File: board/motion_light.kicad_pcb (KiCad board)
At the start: 2 copper layers, 35 x 63.2 mm, 18 parts, among them CON1 AVR-ISP-6, J1 MOTION, J2 Conn_02x03_Counter_Clockwise, SW1 SW_Push, SW2 SW_Push, U1 ATTINY84-SSU, U2 APA102, U3 APA102, U4 PIR_MODULE

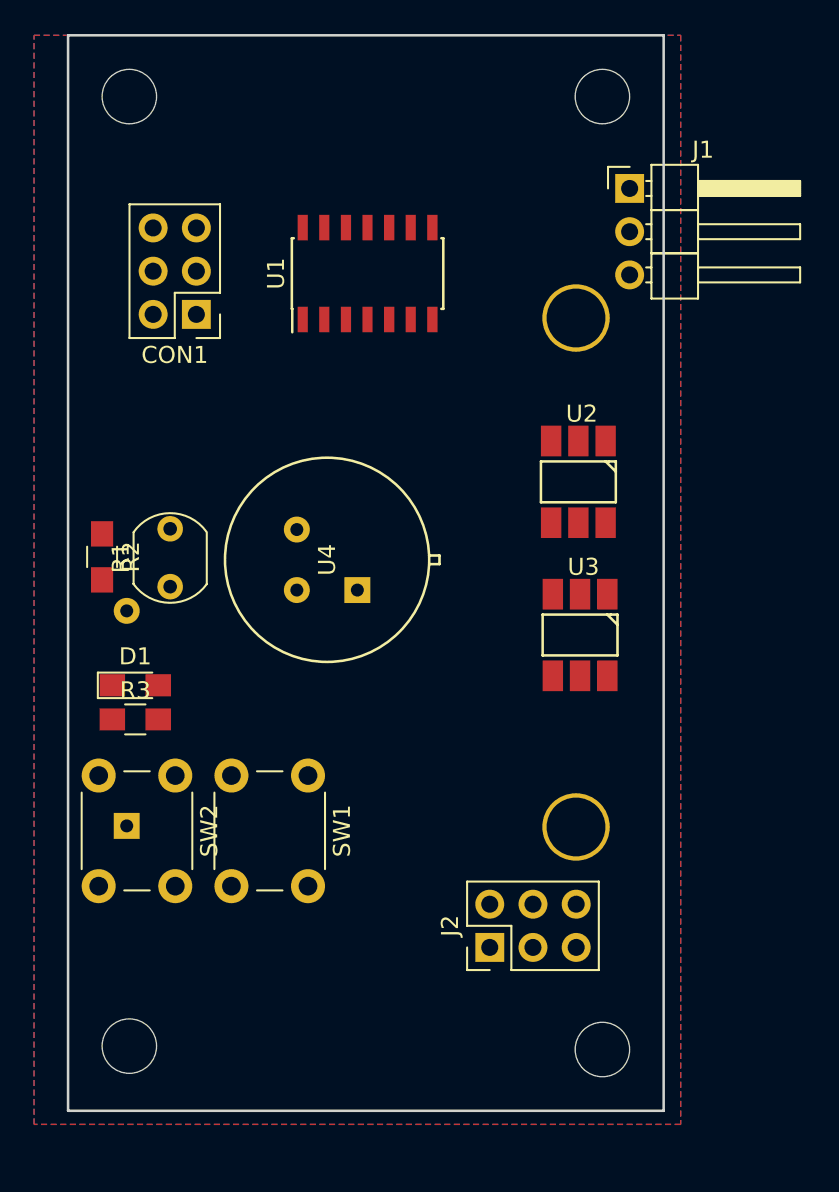
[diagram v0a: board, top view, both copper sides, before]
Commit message: Rework board; add mesh design
* Make board an even size
* Adjust position of motion detector
* Improve model of PIR sensor
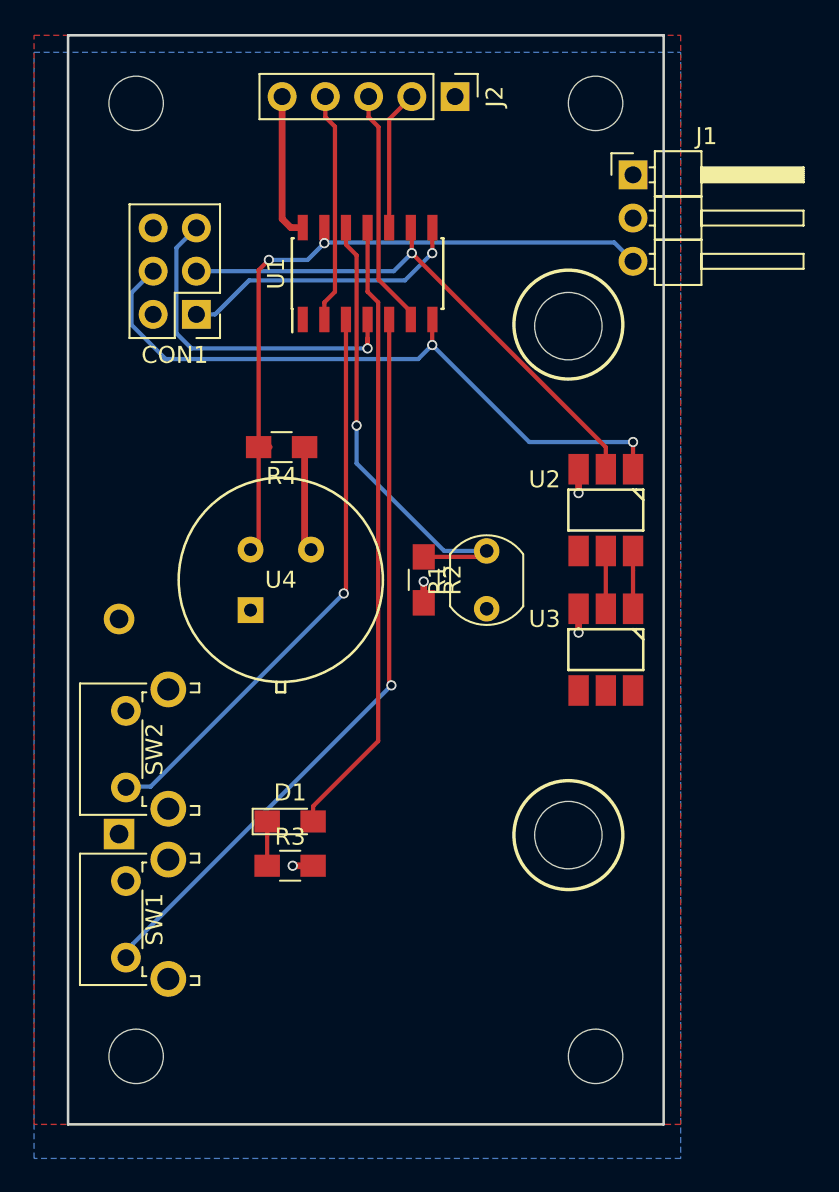
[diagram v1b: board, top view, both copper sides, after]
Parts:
- added R4: 66.5K, Resistors_SMD:R_0805_HandSoldering, F.Cu at (126.5, 84.2)
- J2: value Conn_02x03_Counter_Clockwise -> Conn_01x05; footprint Pin_Headers:Pin_Header_Straight_2x03_Pitch2.54mm -> Pin_Headers:Pin_Header_Straight_1x05_Pitch2.54mm
- SW1, SW2: footprint Buttons_Switches_THT:SW_PUSH_6mm -> Buttons_Switches_THT:SW_Tactile_SPST_Angled_PTS645Vx83-2LFS
- U1: value ATTINY84-SSU -> ATTINY84A-SSU
- moved J2 50.0 mm to (136.7, 63.6), turned to 270 degrees
- moved R2 18.9 mm to (134.9, 92.0)
- moved R1 18.6 mm to (138.6, 93.7)
- moved SW1 15.1 mm to (117.4, 114.2), turned to 90 degrees
- moved R3 12.5 mm to (127.0, 108.8)
- moved D1 12.1 mm to (127.0, 106.2)
- moved SW2 2.98 mm to (117.4, 104.2), turned to 90 degrees
- moved U4 2.97 mm to (126.5, 92.0), turned to 180 degrees
- moved U2 2.31 mm to (145.6, 87.9)
- moved U3 1.74 mm to (145.6, 96.1)
- moved J1 0.82 mm to (147.2, 68.2)
- moved REF** 0.72 mm to (118.0, 120.0)
- moved BT1 0.66 mm to (143.4, 92.0)
- moved REF** 0.57 mm to (145.0, 120.0)
- moved REF** 0.57 mm to (145.0, 64.0)
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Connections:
- J2 pad 4: GND -> /PB0
- J2 pad 5: /PB0 -> GND
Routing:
- net /BUTTON1: track 0.00 -> 43.4 mm, vias 0 -> 1
- net /MOTION: track 0.00 -> 41.3 mm, vias 0 -> 2
- net /SDA: track 0.00 -> 39.8 mm, vias 0 -> 2
- net /STATUS_LED: track 0.00 -> 36.7 mm
- net /BUTTON2: track 0.00 -> 33.3 mm, vias 0 -> 1
- net /SCK: track 0.00 -> 32.8 mm, vias 0 -> 1
- net /AMBIENT: track 0.00 -> 28.2 mm, vias 0 -> 1
- net /RESET: track 0.00 -> 20.6 mm, vias 0 -> 1
- net GND: track 0.00 -> 20.0 mm, vias 0 -> 4
- net /MISO: track 0.00 -> 16.9 mm, vias 0 -> 1
- net /PA7: track 0.00 -> 14.1 mm
- net /PB0: track 0.00 -> 13.6 mm
- net /PA3: track 0.00 -> 8.25 mm
- net Net-(U2-Pad6): track 0.00 -> 3.40 mm
- net Net-(U2-Pad5): track 0.00 -> 3.40 mm
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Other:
- board size 35 x 63.2 mm -> 35 x 64 mm

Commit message: Move ambient light sensor; center buttons and status LED
* Improve silk documentation
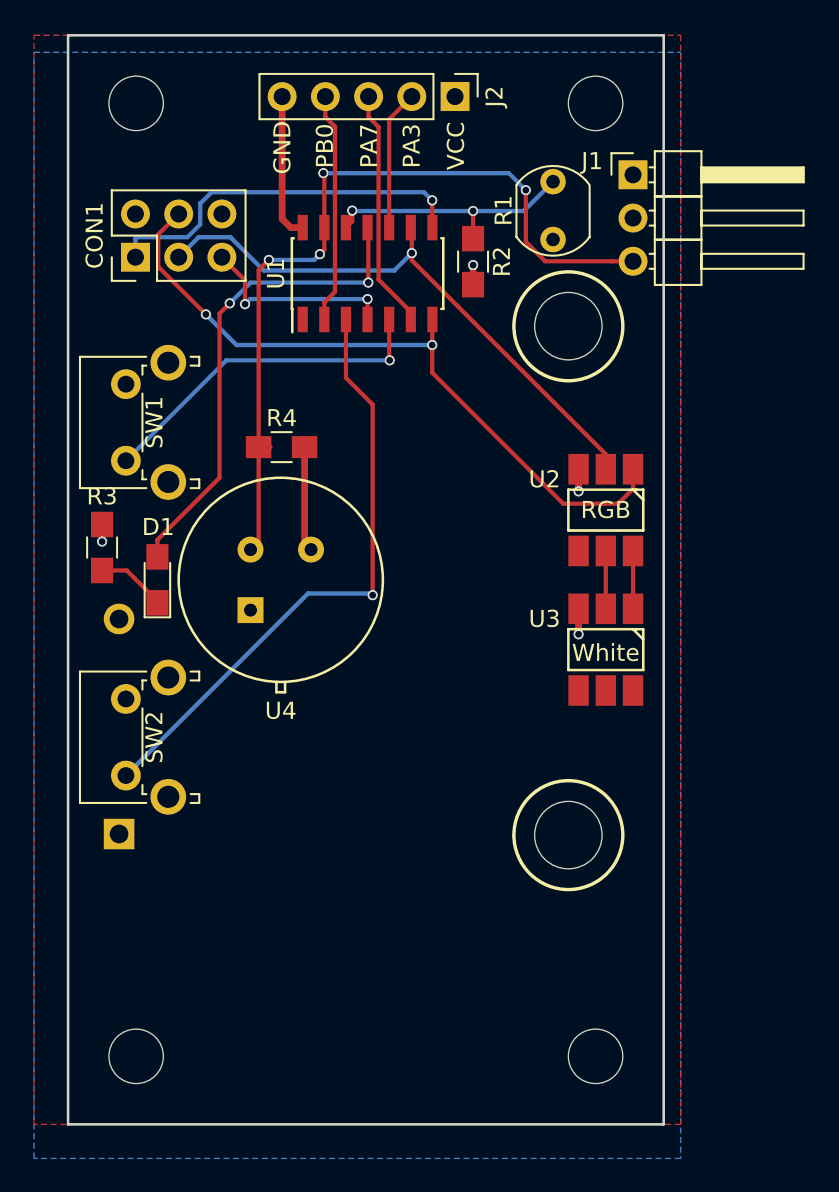
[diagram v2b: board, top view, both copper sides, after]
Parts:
- J1: value MOTION -> MOTION (optional)
- J2: value Conn_01x05 -> GPIO
- REF** (x4): value MountingHole_3.2mm_M3 -> 3.2mm_M3
- moved SW1 29.2 mm to (117.4, 85.0)
- moved R1 22.0 mm to (142.5, 72.0)
- moved R3 21.7 mm to (116.0, 90.1), turned to 90 degrees
- moved R2 18.9 mm to (137.8, 73.3)
- moved D1 16.2 mm to (119.2, 92.0), turned to 90 degrees
- moved CON1 4.91 mm to (118.0, 73.0), turned to 90 degrees
- moved SW2 0.70 mm to (117.4, 103.5)
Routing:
- net /BUTTON1: track 43.4 -> 20.4 mm
- net /AMBIENT: track 28.2 -> 16.4 mm, vias 1 -> 2
- net /RESET: track 20.6 -> 11.8 mm, vias 1 -> 2
- net /STATUS_LED: track 36.7 -> 28.6 mm, vias 0 -> 2
- net /MOTION: track 41.3 -> 48.2 mm, vias 2 -> 4
- net /MISO: track 16.9 -> 22.2 mm
- net /BUTTON2: track 33.3 -> 35.8 mm
- net /SCK: track 32.8 -> 34.4 mm
- net Net-(D1-Pad1): track 2.60 -> 4.10 mm
- net /SDA: track 39.8 -> 41.2 mm
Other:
- board text added: "GND"
- board text added: "PA3"
- board text added: "PA7"
- board text added: "PB0"
- board text added: "RGB"
- board text added: "VCC"
- board text added: "White"

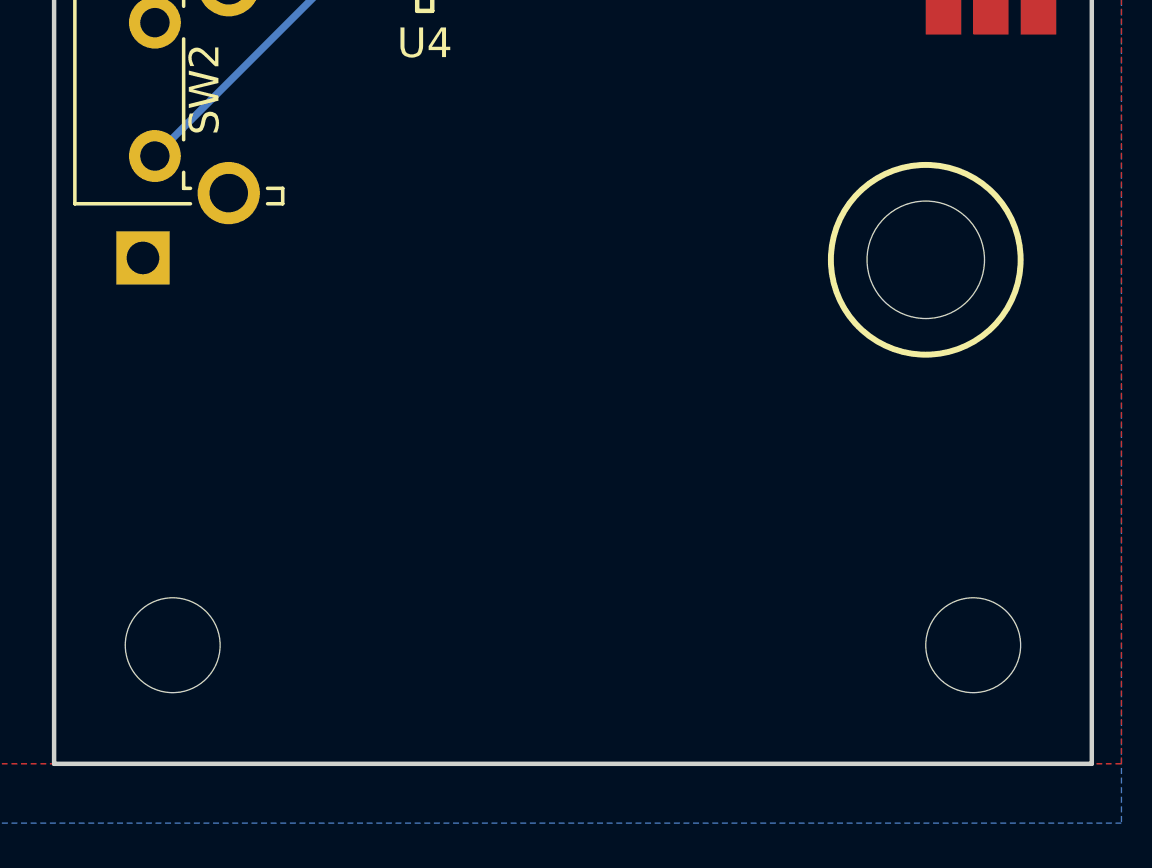
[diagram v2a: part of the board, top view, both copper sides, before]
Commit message: Add more silk docs
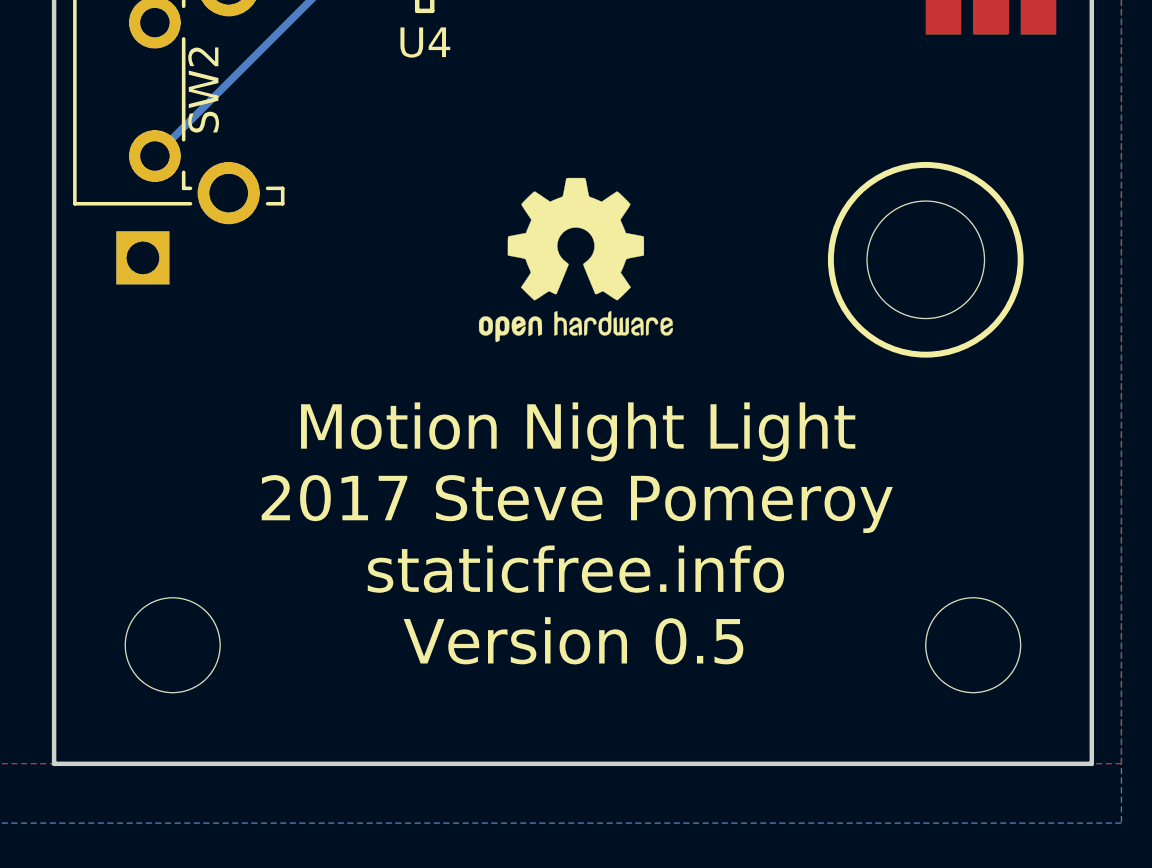
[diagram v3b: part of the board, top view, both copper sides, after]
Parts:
- added REF***: OSHW-Logo2_7.3x6mm_SilkScreen, Symbols:OSHW-Logo2_7.3x6mm_SilkScreen, F.Cu at (131.6, 107.0)
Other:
- board text added: "Motion Night Light 2017 Steve Pomeroy staticfree.info Version 0.5"

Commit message: Fix PIR sensor footprint
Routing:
- net GND: track 19.7 -> 14.7 mm, vias 4 -> 5
- net VCC: track 0.00 -> 0.53 mm
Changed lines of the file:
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@@
 (kicad_pcb (version 4) (host pcbnew 4.0.7+dfsg1-1)
   (general
-    (links 0)
+    (links 40)
     (no_connects 0)
-    (area 113.924999 59.924999 149.075001 124.075001)
+    (area 84.150001 53.05 202.15 137.151426)
     (thickness 1.6)
-    (drawings 17)
-    (tracks 134)
+    (drawings 20)
+    (tracks 136)
     (zones 0)
     (modules 20)
@@
       (rotate (xyz 0 0 0))
     )
-  )
-  (module StaticfreeFootprints:PaPIR_PIR_SENSOR (layer F.Cu)
-    (at 126.5 92 180)
-    (fp_text reference U4 (at 0 -7.7 180) (layer F.SilkS)
-      (effects (font (size 1 1) (thickness 0.15)))
-    )
-    (fp_text value PIR_MODULE (at -2.1 -6.8 180) (layer F.Fab)
-      (effects (font (size 1 1) (thickness 0.15)))
-    )
-    (fp_circle (center 0 0) (end 5.5 0) (layer F.Fab) (width 0.15))
-    (fp_line (start -0.254 -6.604) (end -0.254 -5.9944) (layer F.SilkS) (width 0.15))
-    (fp_line (start 0.254 -6.604) (end -0.254 -6.604) (layer F.SilkS) (width 0.15))
-    (fp_line (start 0.254 -5.9944) (end 0.254 -6.604) (layer F.SilkS) (width 0.15))
-    (fp_circle (center 0 0) (end 6 0) (layer F.SilkS) (width 0.15))
-    (pad 1 thru_hole rect (at 1.778 -1.778 180) (size 1.524 1.524) (drill 0.762) (layers *.Cu *.Mask)
-      (net 1 VCC))
-    (pad 2 thru_hole circle (at 1.778 1.778 180) (size 1.524 1.524) (drill 0.762) (layers *.Cu *.Mask)
-      (net 6 /MOTION))
-    (pad 3 thru_hole circle (at -1.778 1.778 180) (size 1.524 1.524) (drill 0.762) (layers *.Cu *.Mask)
-      (net 5 GND))
   )
   (module Resistors_SMD:R_0805_HandSoldering (layer F.Cu)
@@
       (xy -0.113933 -2.757629) (xy -0.013056 -2.757714) (xy 0 -2.757714) (xy 0.10391 -2.757652)) (layer F.SilkS) (width 0.01))
   )
+  (module StaticfreeFootprints:PaPIR_PIR_SENSOR (layer F.Cu)
+    (at 126.5 92 180)
+    (fp_text reference U4 (at 0 -7.7 180) (layer F.SilkS)
+      (effects (font (size 1 1) (thickness 0.15)))
+    )
+    (fp_text value PIR_MODULE (at -2.1 -6.8 180) (layer F.Fab)
+      (effects (font (size 1 1) (thickness 0.15)))
+    )
+    (fp_circle (center 0 0) (end 5.5 0) (layer F.Fab) (width 0.15))
+    (fp_line (start -0.254 -6.604) (end -0.254 -5.9944) (layer F.SilkS) (width 0.15))
+    (fp_line (start 0.254 -6.604) (end -0.254 -6.604) (layer F.SilkS) (width 0.15))
+    (fp_line (start 0.254 -5.9944) (end 0.254 -6.604) (layer F.SilkS) (width 0.15))
+    (fp_circle (center 0 0) (end 6 0) (layer F.SilkS) (width 0.15))
+    (pad 3 thru_hole circle (at 1.778 -1.778 180) (size 1.524 1.524) (drill 0.762) (layers *.Cu *.Mask)
+      (net 5 GND))
+    (pad 2 thru_hole circle (at 1.778 1.778 180) (size 1.524 1.524) (drill 0.762) (layers *.Cu *.Mask)
+      (net 6 /MOTION))
+    (pad 1 thru_hole rect (at -1.778 1.778 180) (size 1.524 1.524) (drill 0.762) (layers *.Cu *.Mask)
+      (net 1 VCC))
+  )
+  (dimension 4 (width 0.3) (layer Dwgs.User)
+    (gr_text "4.000 mm" (at 107.4 62 90) (layer Dwgs.User)
+      (effects (font (size 1.5 1.5) (thickness 0.3)))
+    )
+    (feature1 (pts (xy 118 60) (xy 106.05 60)))
+    (feature2 (pts (xy 118 64) (xy 106.05 64)))
+    (crossbar (pts (xy 108.75 64) (xy 108.75 60)))
+    (arrow1a (pts (xy 108.75 60) (xy 109.336421 61.126504)))
+    (arrow1b (pts (xy 108.75 60) (xy 108.163579 61.126504)))
+    (arrow2a (pts (xy 108.75 64) (xy 109.336421 62.873496)))
+    (arrow2b (pts (xy 108.75 64) (xy 108.163579 62.873496)))
+  )
+  (dimension 4 (width 0.3) (layer Dwgs.User)
+    (gr_text "4.000 mm" (at 116 54.4) (layer Dwgs.User)
+      (effects (font (size 1.5 1.5) (thickness 0.3)))
+    )
+    (feature1 (pts (xy 114 64) (xy 114 53.05)))
+    (feature2 (pts (xy 118 64) (xy 118 53.05)))
+    (crossbar (pts (xy 118 55.75) (xy 114 55.75)))
+    (arrow1a (pts (xy 114 55.75) (xy 115.126504 55.163579)))
+    (arrow1b (pts (xy 114 55.75) (xy 115.126504 56.336421)))
+    (arrow2a (pts (xy 118 55.75) (xy 116.873496 55.163579)))
+    (arrow2b (pts (xy 118 55.75) (xy 116.873496 56.336421)))
+  )
+  (dimension 9.25 (width 0.3) (layer Dwgs.User)
+    (gr_text "9.250 mm" (at 102.65 87.375 270) (layer Dwgs.User)
+      (effects (font (size 1.5 1.5) (thickness 0.3)))
+    )
+    (feature1 (pts (xy 109 92) (xy 101.3 92)))
+    (feature2 (pts (xy 109 82.75) (xy 101.3 82.75)))
+    (crossbar (pts (xy 104 82.75) (xy 104 92)))
+    (arrow1a (pts (xy 104 92) (xy 103.413579 90.873496)))
+    (arrow1b (pts (xy 104 92) (xy 104.586421 90.873496)))
+    (arrow2a (pts (xy 104 82.75) (xy 103.413579 83.876504)))
+    (arrow2b (pts (xy 104 82.75) (xy 104.586421 83.876504)))
+  )
   (gr_text "Motion Night Light\n2017 Steve Pomeroy\nstaticfree.info\nVersion 0.5" (at 131.6 116.3) (layer F.SilkS)
     (effects (font (size 1.5 1.5) (thickness 0.3)))
@@
   (gr_line (start 149 60) (end 149 124) (layer Edge.Cuts) (width 0.15))
   (gr_line (start 114 60) (end 149 60) (layer Edge.Cuts) (width 0.15))
+  (segment (start 127.9 89.844) (end 128.278 90.222) (width 0.4) (layer F.Cu) (net 1) (status 30))
   (segment (start 145.6 85.5) (end 145.6 84.624264) (width 0.25) (layer F.Cu) (net 2))
   (segment (start 145.6 84.624264) (end 134.2 73.224264) (width 0.25) (layer F.Cu) (net 2))
@@
   (segment (start 131.6 76.7) (end 131.6 75.5) (width 0.25) (layer F.Cu) (net 4) (status 10))
   (via (at 131.6 75.5) (size 0.6) (drill 0.4) (layers F.Cu B.Cu) (net 4))
+  (segment (start 127.9 84.2) (end 126.8 84.2) (width 0.4) (layer F.Cu) (net 5))
+  (segment (start 126.8 84.2) (end 126.75 84.25) (width 0.4) (layer F.Cu) (net 5))
+  (via (at 126.75 84.25) (size 0.6) (drill 0.4) (layers F.Cu B.Cu) (net 5))
   (via (at 137.8 73.5) (size 0.6) (drill 0.4) (layers F.Cu B.Cu) (net 5))
   (segment (start 137.8 74.65) (end 137.8 73.5) (width 0.4) (layer F.Cu) (net 5) (status 10))
@@
   (segment (start 116 88.75) (end 116 89.75) (width 0.4) (layer F.Cu) (net 5) (status 10))
   (via (at 116 89.75) (size 0.6) (drill 0.4) (layers F.Cu B.Cu) (net 5))
-  (segment (start 127.9 84.2) (end 127.9 89.844) (width 0.4) (layer F.Cu) (net 5) (status 30))
-  (segment (start 127.9 89.844) (end 128.278 90.222) (width 0.4) (layer F.Cu) (net 5) (status 30))
   (segment (start 126.58 63.6) (end 126.58 70.79) (width 0.4) (layer F.Cu) (net 5) (status 10))
   (segment (start 126.58 70.79) (end 127.09 71.3) (width 0.4) (layer F.Cu) (net 5))
